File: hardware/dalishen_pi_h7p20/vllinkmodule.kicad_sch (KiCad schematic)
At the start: 30 parts, among them J1001 USB_C_Receptacle_USB2.0_16P, U1001 AIC8800FC, U1002 P25Q80H/P25Q64H/P25Q128HA, Y1001 26M, 10PPM

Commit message: [dalishen_pi_h7p20] 原理图预审
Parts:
- C1002: value 1.3pF -> NC
- C1011: value 10uF -> NC
- L1001: value 1.4nH -> 0R
- L1003: value 1.8nH -> 0R
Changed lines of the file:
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@@
       (effects (font (size 1.27 1.27)))
     )
-    (property "Value" "1.4nH" (at 40.64 128.2954 90)
+    (property "Value" "0R" (at 40.64 128.2954 90)
       (effects (font (size 1.27 1.27)))
     )
@@
       (effects (font (size 1.27 1.27)) (justify left))
     )
-    (property "Value" "1.3pF" (at 47.371 106.553 0)
+    (property "Value" "NC" (at 47.371 106.553 0)
       (effects (font (size 1.27 1.27)) (justify left))
     )
@@
       (effects (font (size 1.27 1.27)) (justify left))
     )
-    (property "Value" "10uF" (at 117.221 111.633 0)
+    (property "Value" "NC" (at 117.221 111.633 0)
       (effects (font (size 1.27 1.27)) (justify left))
     )
@@
       (effects (font (size 1.27 1.27)))
     )
-    (property "Value" "1.8nH" (at 49.53 99.0854 90)
-      (effects (font (size 1.27 1.27)))
-    )
+    (property "Value" "0R" (at 49.53 99.0854 90)
+      (effects (font (size 1.27 1.27)))
+    )

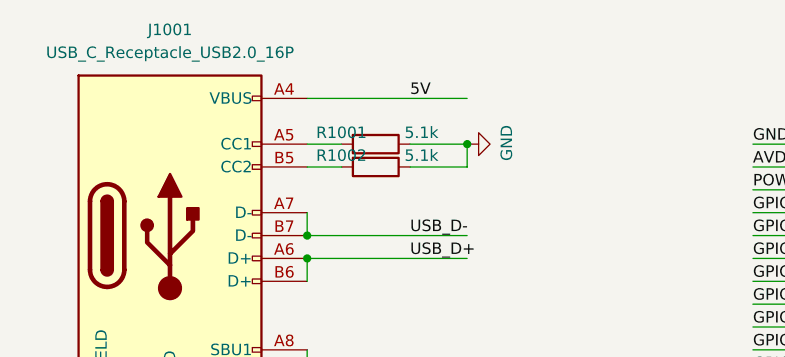
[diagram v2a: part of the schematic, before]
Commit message: [dalishen_pi_h7p20] production_files.20250820 新增保险丝
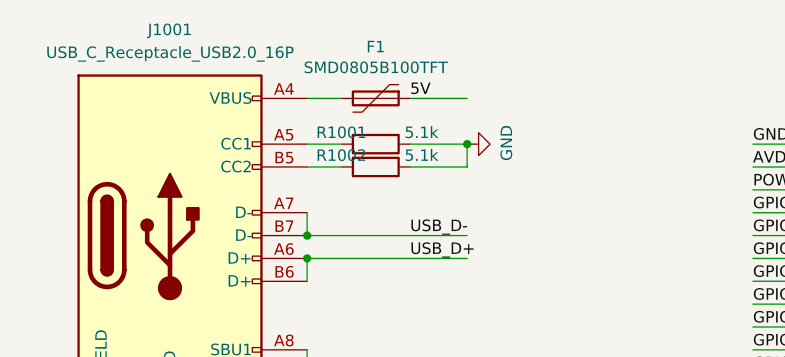
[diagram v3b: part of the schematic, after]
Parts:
- added F1: SMD0805B100TFT, Fuse:Fuse_0805_2012Metric, symbol Device:Polyfuse
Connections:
- net VL_5V: now also F1.1; no longer J1001.A4 (VBUS), J1001.A9 (VBUS), J1001.B4 (VBUS), J1001.B9 (VBUS)
- new net: F1.2, J1001.A4 (VBUS), J1001.A9 (VBUS), J1001.B4 (VBUS), J1001.B9 (VBUS)
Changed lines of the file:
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@@
 	(wire
 		(pts
-			(xy 58.42 24.13) (xy 76.2 24.13)
+			(xy 58.42 24.13) (xy 62.23 24.13)
 		)
 		(stroke
@@
 		(pts
 			(xy 99.06 130.81) (xy 124.46 130.81)
+		)
+		(stroke
+			(width 0)
+			(type default)
+		)
+	)
+	(wire
+		(pts
+			(xy 69.85 24.13) (xy 76.2 24.13)
 		)
 		(stroke
@@
 		)
 	)
+	(symbol
+		(lib_id "Device:Polyfuse")
+		(at 66.04 24.13 270)
+		(unit 1)
+		(exclude_from_sim no)
+		(in_bom yes)
+		(on_board yes)
+		(dnp no)
+		(property "Reference" "F1"
+			(at 66.04 18.415 90)
+			(effects
+				(font
+					(size 1.27 1.27)
+				)
+			)
+		)
+		(property "Value" "SMD0805B100TFT"
+			(at 66.04 20.7264 90)
+			(effects
+				(font
+					(size 1.27 1.27)
+				)
+			)
+		)
+		(property "Footprint" "Fuse:Fuse_0805_2012Metric"
+			(at 60.96 25.4 0)
+			(effects
+				(font
+					(size 1.27 1.27)
+				)
+				(justify left)
+				(hide yes)
+			)
+		)
+		(property "Datasheet" "~"
+			(at 66.04 24.13 0)
+			(effects
+				(font
+					(size 1.27 1.27)
+				)
+				(hide yes)
+			)
+		)
+		(property "Description" ""
+			(at 66.04 24.13 0)
+			(effects
+				(font
+					(size 1.27 1.27)
+				)
+			)
+		)
+		(pin "1"
+		)
+		(pin "2"
+		)
+		(instances
+			(project "dalishen_pi_h7p20"
+				(path "/221176f3-b6da-4f04-afa6-f8c6dd49907a/7107c972-7697-471f-a4f8-9040c1889bdb"
+					(reference "F1")
+					(unit 1)
+				)
+			)
+		)
+	)

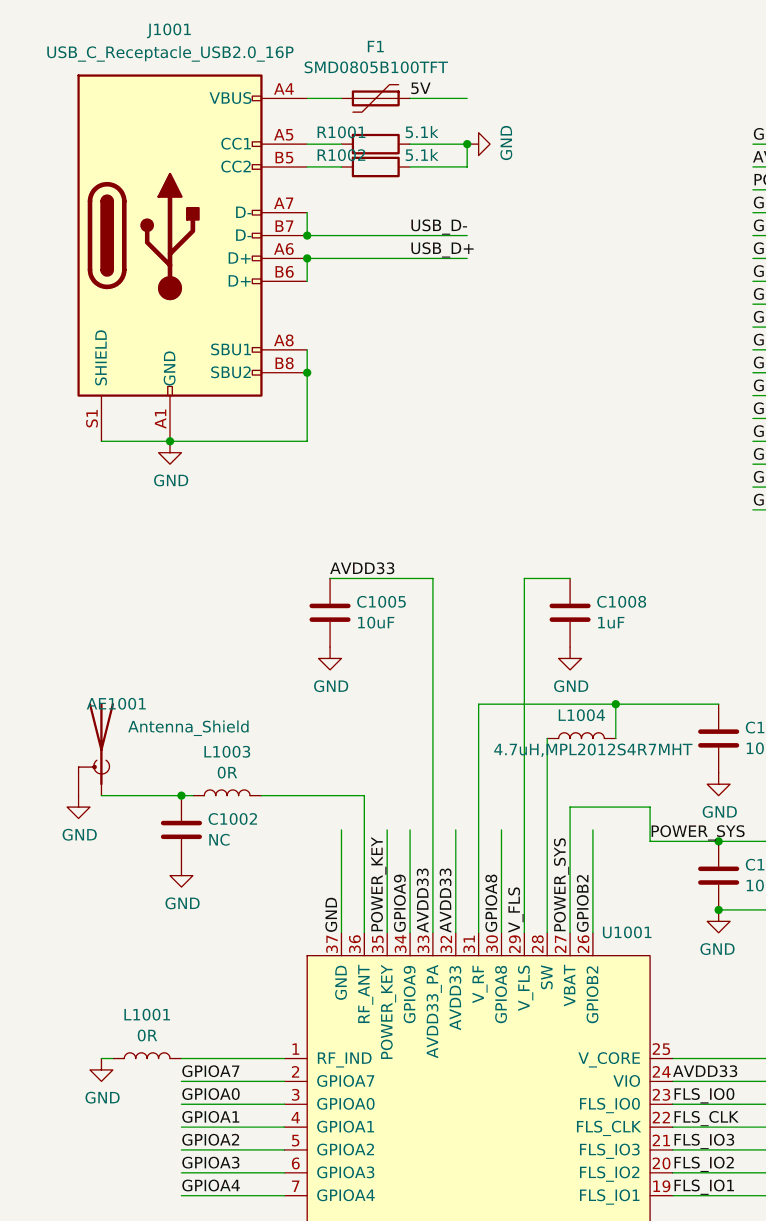
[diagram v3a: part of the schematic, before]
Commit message: [dalishen_pi_h7p20] 生成方波
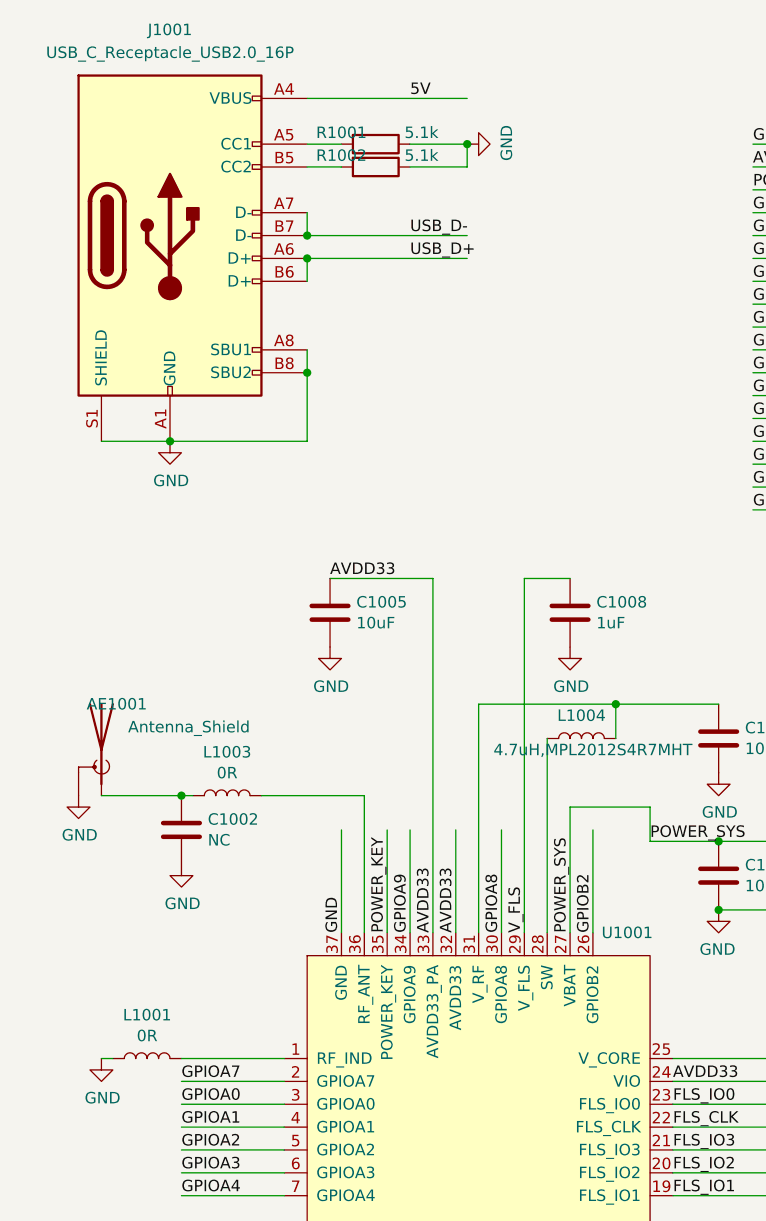
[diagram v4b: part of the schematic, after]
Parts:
- removed F1: SMD0805B100TFT, Fuse:Fuse_0805_2012Metric, symbol Device:Polyfuse
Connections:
- net VL_5V: now also J1001.A4 (VBUS), J1001.A9 (VBUS), J1001.B4 (VBUS), J1001.B9 (VBUS)
